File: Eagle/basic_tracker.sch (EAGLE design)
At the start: 21 parts, among them CN1 BATTERY, IC1 MCP1700 3.3v, X1 SMA

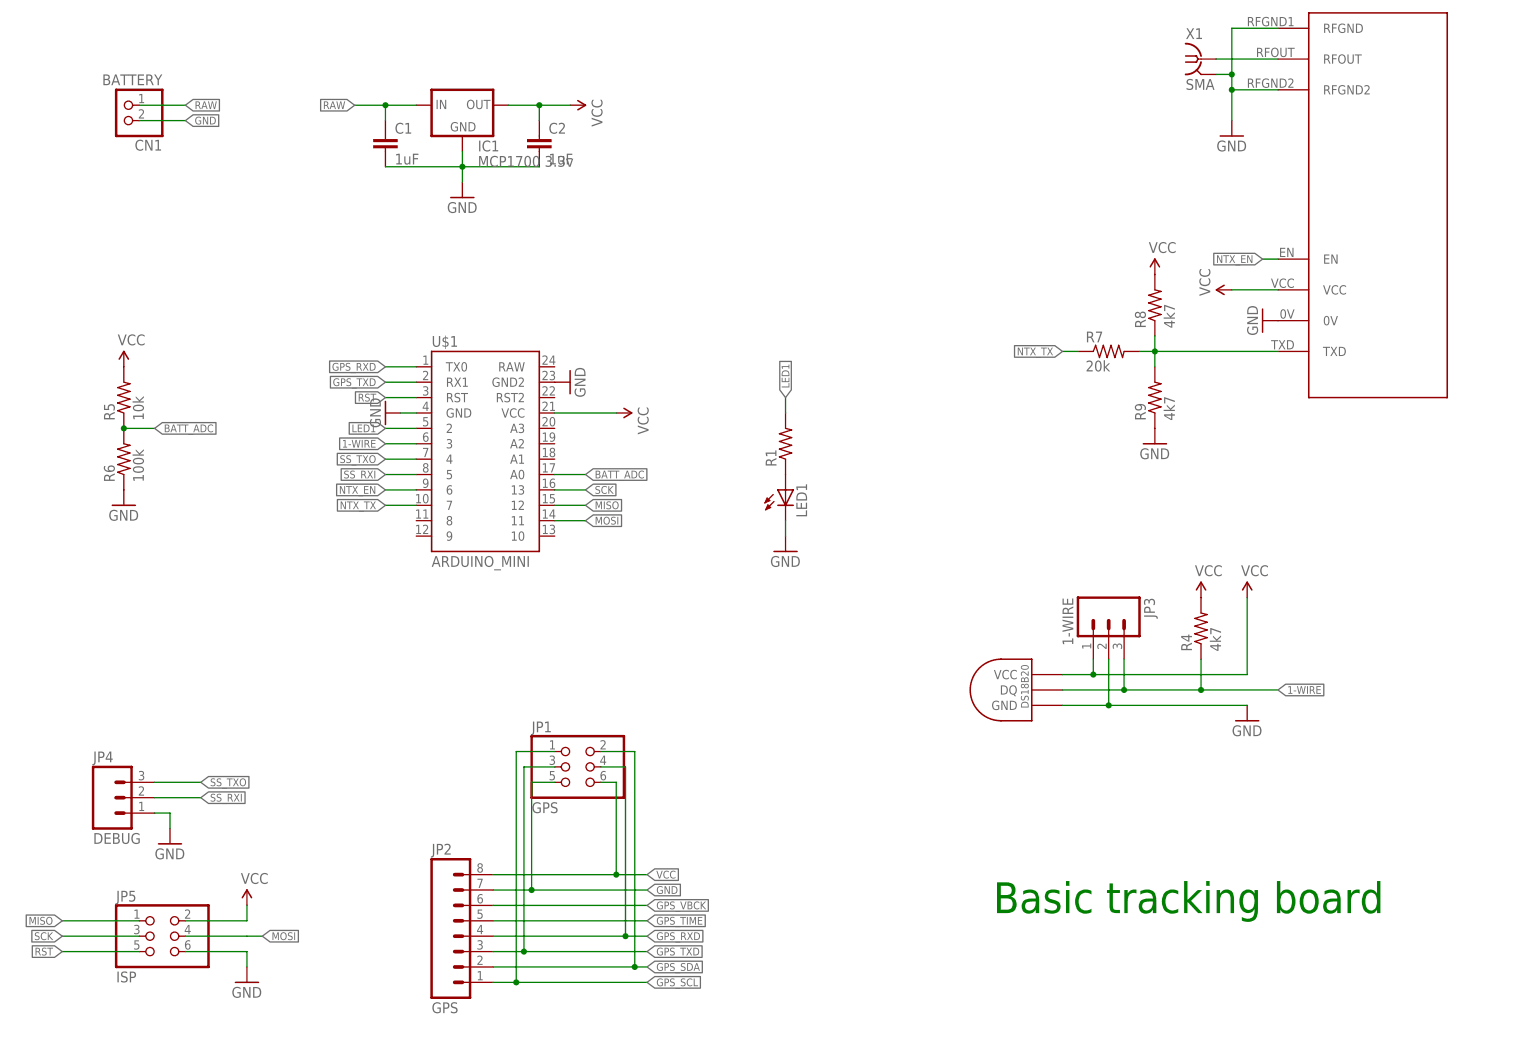
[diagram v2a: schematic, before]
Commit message: Added datasheets and BOM. Fixed issue with v1 PCB
The v1 PCB had an error with the battery voltage monitor - it was eing
fed by Vcc not Vbatt so could only monitor the regulator voltage. Bumped
schematic version to 1.1, board not yet re-routed.
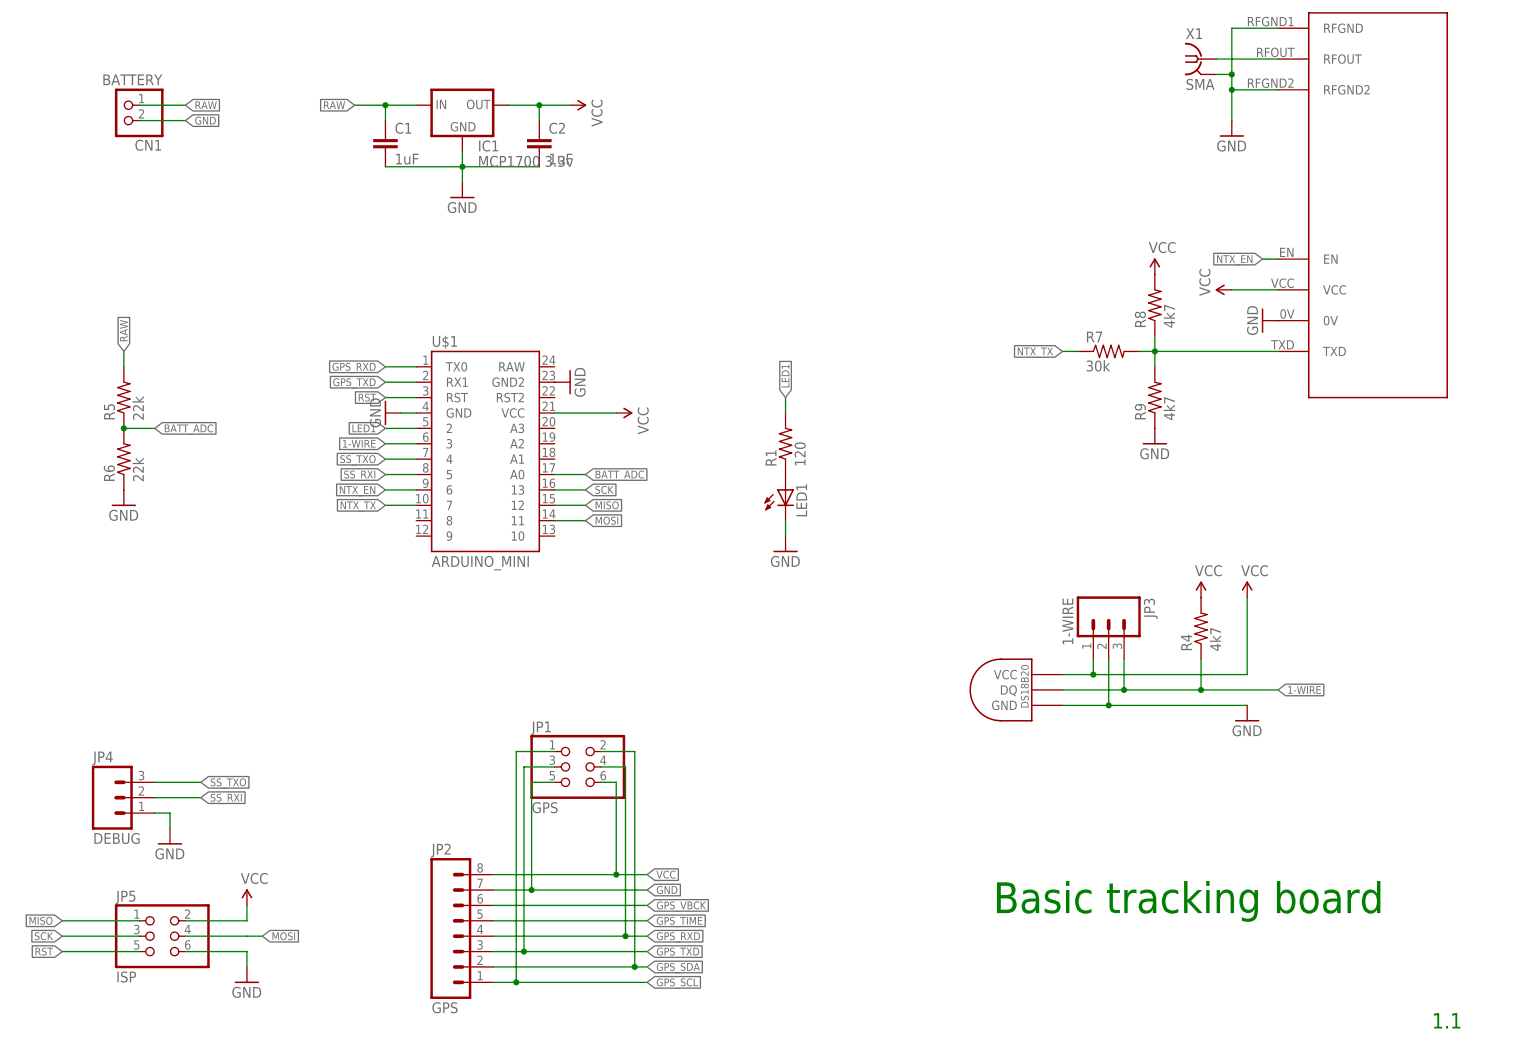
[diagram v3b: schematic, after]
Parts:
- R1: value (none) -> 120
- R5: value 10k -> 22k
- R6: value 100k -> 22k
- R7: value 20k -> 30k
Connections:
- net RAW: now also R5.2
- net VCC: no longer R5.2
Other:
- note added: "1.1"
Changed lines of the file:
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@@
 <grid distance="0.1" unitdist="inch" unit="inch" style="lines" multiple="1" display="no" altdistance="0.01" altunitdist="inch" altunit="inch"/>
 <layers>
-<layer number="1" name="Top" color="4" fill="1" visible="yes" active="no"/>
-<layer number="16" name="Bottom" color="1" fill="1" visible="yes" active="no"/>
-<layer number="17" name="Pads" color="2" fill="1" visible="yes" active="no"/>
-<layer number="18" name="Vias" color="2" fill="1" visible="yes" active="no"/>
-<layer number="19" name="Unrouted" color="6" fill="1" visible="yes" active="no"/>
-<layer number="20" name="Dimension" color="15" fill="1" visible="yes" active="no"/>
-<layer number="21" name="tPlace" color="14" fill="1" visible="yes" active="no"/>
-<layer number="22" name="bPlace" color="7" fill="1" visible="yes" active="no"/>
-<layer number="23" name="tOrigins" color="15" fill="1" visible="yes" active="no"/>
-<layer number="24" name="bOrigins" color="15" fill="1" visible="yes" active="no"/>
-<layer number="25" name="tNames" color="7" fill="1" visible="yes" active="no"/>
-<layer number="26" name="bNames" color="7" fill="1" visible="yes" active="no"/>
-<layer number="27" name="tValues" color="7" fill="1" visible="yes" active="no"/>
-<layer number="28" name="bValues" color="7" fill="1" visible="yes" active="no"/>
+<layer number="1" name="Top" color="4" fill="1" visible="no" active="no"/>
+<layer number="16" name="Bottom" color="1" fill="1" visible="no" active="no"/>
+<layer number="17" name="Pads" color="2" fill="1" visible="no" active="no"/>
+<layer number="18" name="Vias" color="2" fill="1" visible="no" active="no"/>
+<layer number="19" name="Unrouted" color="6" fill="1" visible="no" active="no"/>
+<layer number="20" name="Dimension" color="15" fill="1" visible="no" active="no"/>
+<layer number="21" name="tPlace" color="14" fill="1" visible="no" active="no"/>
+<layer number="22" name="bPlace" color="7" fill="1" visible="no" active="no"/>
+<layer number="23" name="tOrigins" color="15" fill="1" visible="no" active="no"/>
+<layer number="24" name="bOrigins" color="15" fill="1" visible="no" active="no"/>
+<layer number="25" name="tNames" color="7" fill="1" visible="no" active="no"/>
+<layer number="26" name="bNames" color="7" fill="1" visible="no" active="no"/>
+<layer number="27" name="tValues" color="7" fill="1" visible="no" active="no"/>
+<layer number="28" name="bValues" color="7" fill="1" visible="no" active="no"/>
 <layer number="29" name="tStop" color="7" fill="3" visible="no" active="no"/>
 <layer number="30" name="bStop" color="7" fill="6" visible="no" active="no"/>
@@
 <layer number="35" name="tGlue" color="7" fill="4" visible="no" active="no"/>
 <layer number="36" name="bGlue" color="7" fill="5" visible="no" active="no"/>
-<layer number="37" name="tTest" color="7" fill="1" visible="yes" active="no"/>
-<layer number="38" name="bTest" color="7" fill="1" visible="yes" active="no"/>
+<layer number="37" name="tTest" color="7" fill="1" visible="no" active="no"/>
+<layer number="38" name="bTest" color="7" fill="1" visible="no" active="no"/>
 <layer number="39" name="tKeepout" color="4" fill="11" visible="no" active="no"/>
 <layer number="40" name="bKeepout" color="1" fill="11" visible="no" active="no"/>
@@
 <layer number="44" name="Drills" color="7" fill="1" visible="no" active="no"/>
 <layer number="45" name="Holes" color="7" fill="1" visible="no" active="no"/>
-<layer number="46" name="Milling" color="3" fill="1" visible="yes" active="no"/>
-<layer number="47" name="Measures" color="7" fill="1" visible="yes" active="no"/>
-<layer number="48" name="Document" color="7" fill="1" visible="yes" active="no"/>
-<layer number="49" name="Reference" color="7" fill="1" visible="yes" active="no"/>
-<layer number="50" name="dxf" color="7" fill="1" visible="yes" active="no"/>
-<layer number="51" name="tDocu" color="14" fill="1" visible="yes" active="no"/>
-<layer number="52" name="bDocu" color="7" fill="1" visible="yes" active="no"/>
-<layer number="53" name="tGND_GNDA" color="7" fill="9" visible="yes" active="no"/>
-<layer number="54" name="bGND_GNDA" color="1" fill="9" visible="yes" active="no"/>
-<layer number="56" name="wert" color="7" fill="1" visible="yes" active="no"/>
+<layer number="46" name="Milling" color="3" fill="1" visible="no" active="no"/>
+<layer number="47" name="Measures" color="7" fill="1" visible="no" active="no"/>
+<layer number="48" name="Document" color="7" fill="1" visible="no" active="no"/>
+<layer number="49" name="Reference" color="7" fill="1" visible="no" active="no"/>
+<layer number="50" name="dxf" color="7" fill="1" visible="no" active="no"/>
+<layer number="51" name="tDocu" color="14" fill="1" visible="no" active="no"/>
+<layer number="52" name="bDocu" color="7" fill="1" visible="no" active="no"/>
+<layer number="53" name="tGND_GNDA" color="7" fill="9" visible="no" active="no"/>
+<layer number="54" name="bGND_GNDA" color="1" fill="9" visible="no" active="no"/>
+<layer number="56" name="wert" color="7" fill="1" visible="no" active="no"/>
 <layer number="91" name="Nets" color="2" fill="1" visible="yes" active="yes"/>
 <layer number="92" name="Busses" color="1" fill="1" visible="yes" active="yes"/>
@@
 <part name="X1" library="con-coax" deviceset="BU-SMA-H" device="" value="SMA"/>
 <part name="U$3" library="Ava" deviceset="NTX2-VERTICAL" device=""/>
-<part name="R5" library="SparkFun" deviceset="RESISTOR" device="AXIAL-0.3" value="10k"/>
-<part name="R6" library="SparkFun" deviceset="RESISTOR" device="AXIAL-0.3" value="100k"/>
+<part name="R5" library="SparkFun" deviceset="RESISTOR" device="AXIAL-0.3" value="22k"/>
+<part name="R6" library="SparkFun" deviceset="RESISTOR" device="AXIAL-0.3" value="22k"/>
 <part name="JP3" library="SparkFun" deviceset="M03" device="JST-PTH" value="1-WIRE"/>
 <part name="P+1" library="SparkFun" deviceset="VCC" device=""/>
-<part name="P+2" library="SparkFun" deviceset="VCC" device=""/>
 <part name="P+3" library="SparkFun" deviceset="VCC" device=""/>
 <part name="P+4" library="SparkFun" deviceset="VCC" device=""/>
@@
 <part name="GND5" library="SparkFun" deviceset="GND" device=""/>
 <part name="GND6" library="SparkFun" deviceset="GND" device=""/>
-<part name="R7" library="SparkFun" deviceset="RESISTOR" device="AXIAL-0.3" value="20k"/>
+<part name="R7" library="SparkFun" deviceset="RESISTOR" device="AXIAL-0.3" value="30k"/>
 <part name="R8" library="SparkFun" deviceset="RESISTOR" device="AXIAL-0.3" value="4k7"/>
 <part name="R9" library="SparkFun" deviceset="RESISTOR" device="AXIAL-0.3" value="4k7"/>
@@
 <part name="GND9" library="SparkFun" deviceset="GND" device=""/>
 <part name="P+8" library="SparkFun" deviceset="VCC" device=""/>
-<part name="R1" library="SparkFun" deviceset="RESISTOR" device="AXIAL-0.3"/>
+<part name="R1" library="SparkFun" deviceset="RESISTOR" device="AXIAL-0.3" value="120"/>
 <part name="GND10" library="SparkFun" deviceset="GND" device=""/>
 <part name="LED1" library="SparkFun" deviceset="LED" device="3MM"/>
@@
 <plain>
 <text x="181.61" y="26.67" size="5.08" layer="91">Basic tracking board</text>
+<text x="254" y="7.62" size="2.54" layer="91">1.1</text>
 </plain>
 <instances>
@@
 <instance part="JP3" gate="G$1" x="200.66" y="76.2" rot="R270"/>
 <instance part="P+1" gate="1" x="223.52" y="78.74"/>
-<instance part="P+2" gate="1" x="38.1" y="116.84"/>
 <instance part="P+3" gate="1" x="215.9" y="78.74"/>
 <instance part="P+4" gate="1" x="220.98" y="129.54" rot="R90"/>
@@
 <net name="VCC" class="0">
 <segment>
-<pinref part="R5" gate="G$1" pin="2"/>
-<pinref part="P+2" gate="1" pin="VCC"/>
-</segment>
-<segment>
 <pinref part="R4" gate="G$1" pin="2"/>
 <pinref part="P+3" gate="1" pin="VCC"/>
@@
 <label x="48.26" y="160.02" size="1.27" layer="95" xref="yes"/>
 </segment>
-</net>
+<segment>
+<pinref part="R5" gate="G$1" pin="2"/>
+<wire x1="38.1" y1="116.84" x2="38.1" y2="119.38" width="0.1524" layer="91"/>
+<label x="38.1" y="119.38" size="1.27" layer="95" rot="R90" xref="yes"/>
+</segment>
+</net>
